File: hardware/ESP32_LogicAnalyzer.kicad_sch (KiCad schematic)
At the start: 12 parts, among them J1 Conn_01x15, J2 Conn_01x15, J5 DEBUG, J6 CHANNELS, U1 SN74LVC245APW, U2 SN74LVC245APW

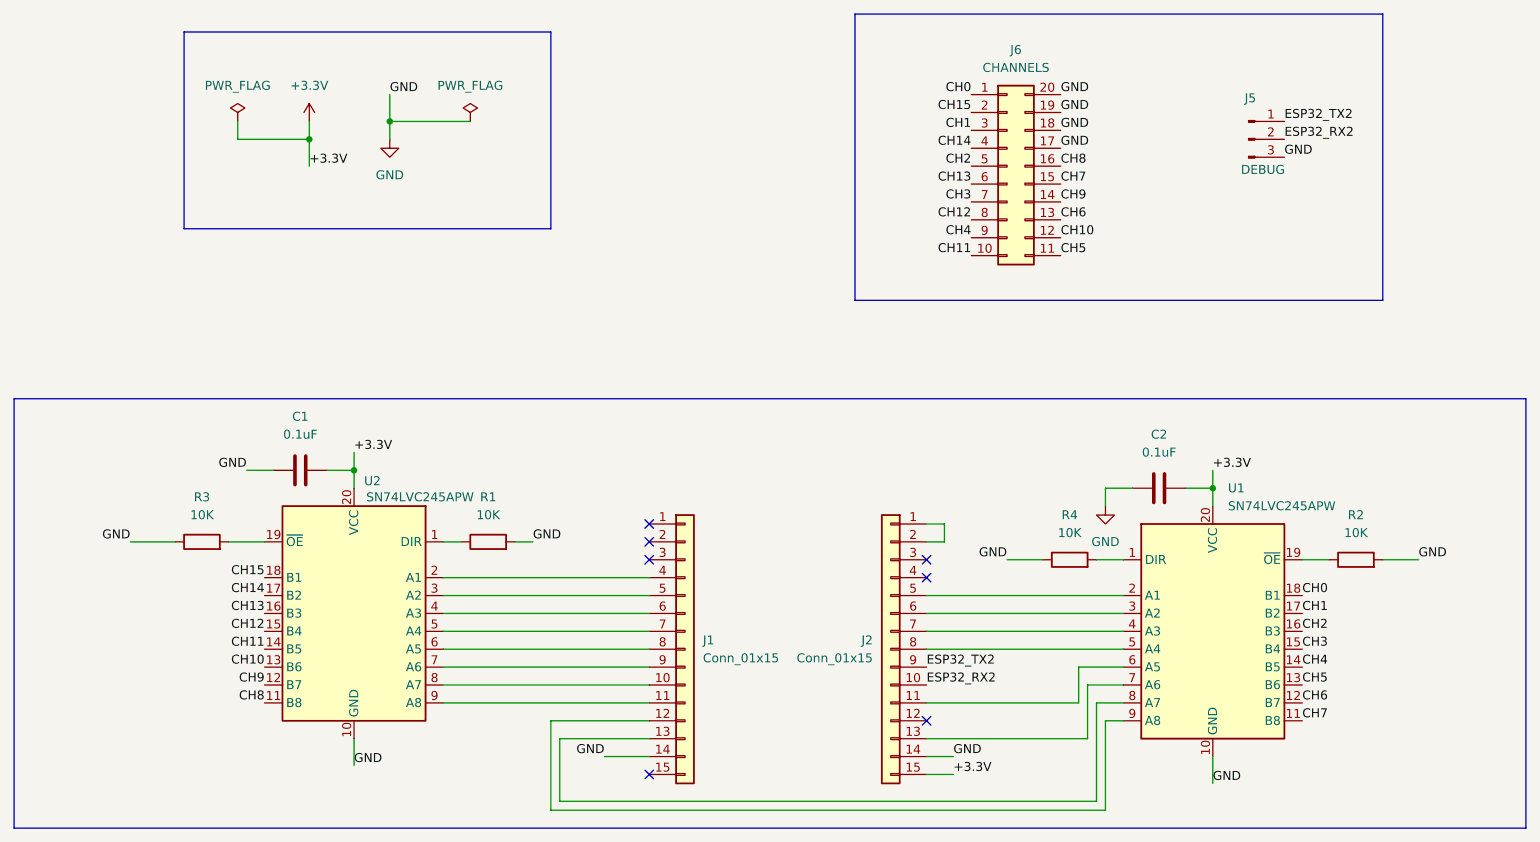
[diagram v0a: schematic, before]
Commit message: Update ESP32 PCB hardware files
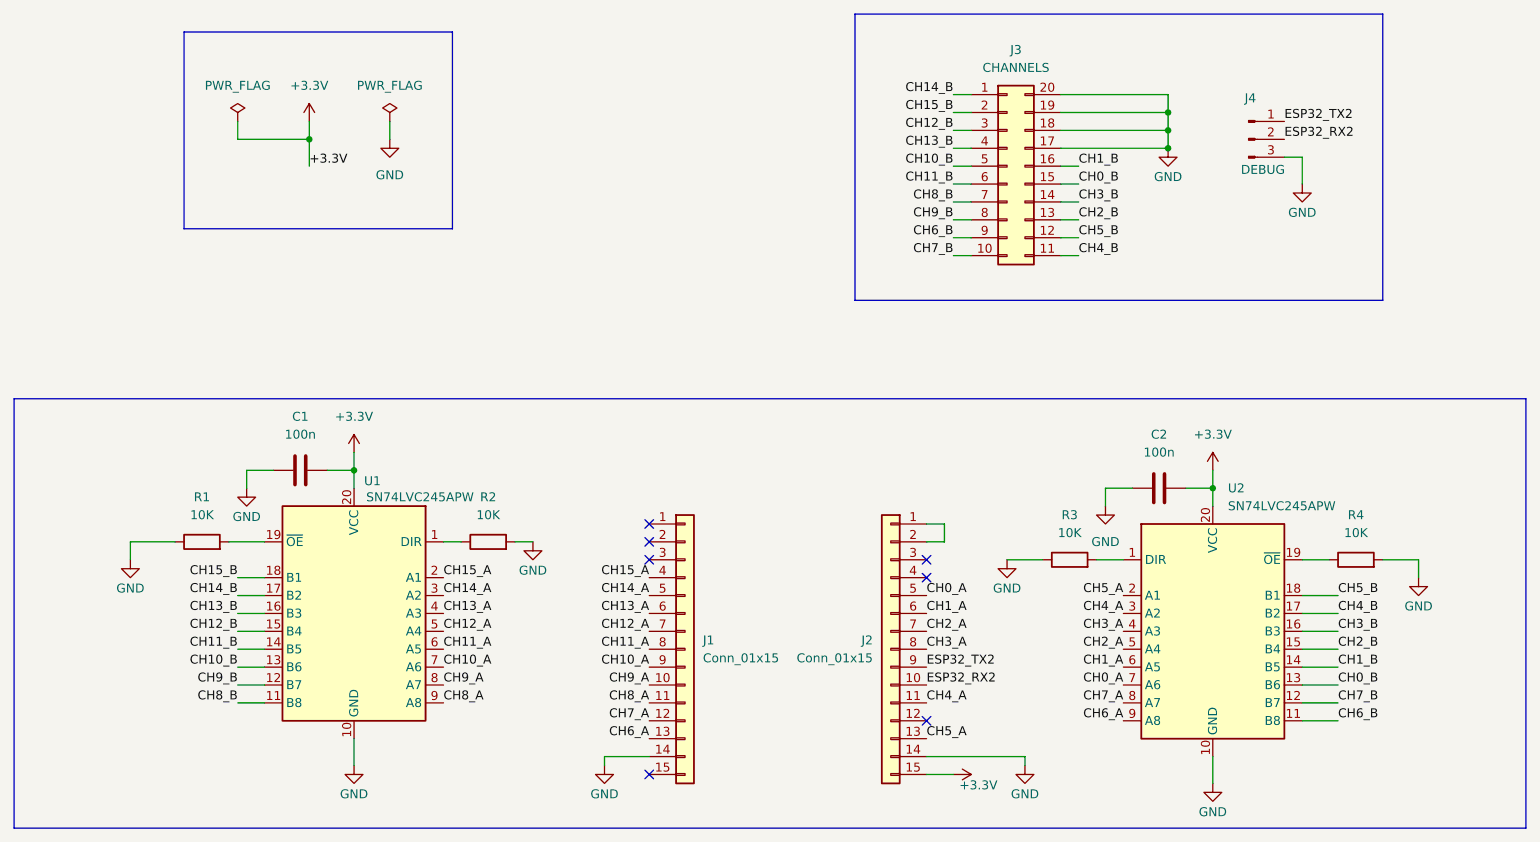
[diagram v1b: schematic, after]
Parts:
- C1, C2: value 0.1uF -> 100n; footprint Capacitor_SMD:C_0805_2012Metric -> Capacitor_SMD:C_0603_1608Metric
- R1: renamed from R3; footprint Resistor_SMD:R_0805_2012Metric -> Resistor_SMD:R_0603_1608Metric
- R2: renamed from R1; footprint Resistor_SMD:R_0805_2012Metric -> Resistor_SMD:R_0603_1608Metric
- R3: renamed from R4; footprint Resistor_SMD:R_0805_2012Metric -> Resistor_SMD:R_0603_1608Metric
- R4: renamed from R2; footprint Resistor_SMD:R_0805_2012Metric -> Resistor_SMD:R_0603_1608Metric
- renumbered J6 to J3, J5 to J4, U2 to U1, U1 to U2
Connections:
- net CH15_A: now reaches J1.4 (Pin_4), U1.2 (A1)
- net CH14_A: now reaches J1.5 (Pin_5), U1.3 (A2)
- net CH13_A: now reaches J1.6 (Pin_6), U1.4 (A3)
- net CH12_A: now reaches J1.7 (Pin_7), U1.5 (A4)
- net CH11_A: now reaches J1.8 (Pin_8), U1.6 (A5)
- net CH10_A: now reaches J1.9 (Pin_9), U1.7 (A6)
- net CH9_A: now reaches J1.10 (Pin_10), U1.8 (A7)
- net CH8_A: now reaches J1.11 (Pin_11), U1.9 (A8)
- net CH6_A: now reaches U2.9 (A8)
- net CH6_A: now also J1.13 (Pin_13); no longer J1.12 (Pin_12)
- net CH7_A: now reaches U2.8 (A7)
- net CH7_A: now also J1.12 (Pin_12); no longer J1.13 (Pin_13)
- net CH1_A: now reaches U2.6 (A5)
- net CH1_A: now also J2.6 (Pin_6); no longer J2.11 (Pin_11)
- net CH0_A: now reaches U2.7 (A6)
- net CH0_A: now also J2.5 (Pin_5); no longer J2.13 (Pin_13)
- net CH5_A: now reaches U2.2 (A1)
- net CH5_A: now also J2.13 (Pin_13); no longer J2.5 (Pin_5)
- net CH4_A: now reaches U2.3 (A2)
- net CH4_A: now also J2.11 (Pin_11); no longer J2.6 (Pin_6)
- net CH2_A: now reaches J2.7 (Pin_7)
- net CH2_A: now also U2.5 (A4); no longer U2.4 (A3)
- net CH3_A: now reaches J2.8 (Pin_8)
- net CH3_A: now also U2.4 (A3); no longer U2.5 (A4)
- net CH0 renamed CH14_B
- net CH14_B: now also U1.17 (B2); no longer U2.18 (B1)
- net CH1 renamed CH12_B
- net CH12_B: now also U1.15 (B4); no longer U2.17 (B2)
- net CH10 renamed CH10_B
- net CH10_B: now also J3.5 (Pin_5); no longer J3.12 (Pin_12)
- net CH11 renamed CH11_B
- net CH11_B: now also J3.6 (Pin_6); no longer J3.10 (Pin_10)
- net CH12 renamed CH9_B
- net CH9_B: now also U1.12 (B7); no longer U1.15 (B4)
- net CH13 renamed CH13_B
- net CH13_B: now also J3.4 (Pin_4); no longer J3.6 (Pin_6)
- removed net CH14: J3.4 (Pin_4), U1.17 (B2)
- net CH15 renamed CH15_B
- net CH2 renamed CH3_B
- net CH3_B: now also J3.14 (Pin_14); no longer J3.5 (Pin_5)
- net CH3 renamed CH2_B
- net CH2_B: now also J3.13 (Pin_13); no longer J3.7 (Pin_7)
- net CH4 renamed CH1_B
- net CH1_B: now also J3.16 (Pin_16); no longer J3.9 (Pin_9)
- net CH5 renamed CH0_B
- net CH0_B: now also J3.15 (Pin_15); no longer J3.11 (Pin_11)
- net CH6 renamed CH7_B
- net CH7_B: now also J3.10 (Pin_10); no longer J3.13 (Pin_13)
- net CH7 renamed CH6_B
- net CH6_B: now also J3.9 (Pin_9); no longer J3.15 (Pin_15)
- net CH8 renamed CH8_B
- net CH8_B: now also J3.7 (Pin_7); no longer J3.16 (Pin_16)
- removed net CH9: J3.14 (Pin_14), U1.12 (B7)
- new net CH4_B: J3.11 (Pin_11), U2.17 (B2)
- new net CH5_B: J3.12 (Pin_12), U2.18 (B1)
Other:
- company: lmcapacho -> @LMCapacho
